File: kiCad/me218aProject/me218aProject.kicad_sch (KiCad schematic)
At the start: 22 parts, among them M1 Motor_Servo, M2 Motor_Servo, M3 Motor_Servo, M4 Motor_Servo, SW1 SW-PB, U1 PIC32MX170F256B, U2 74ACT244, U3 LED_Matrix

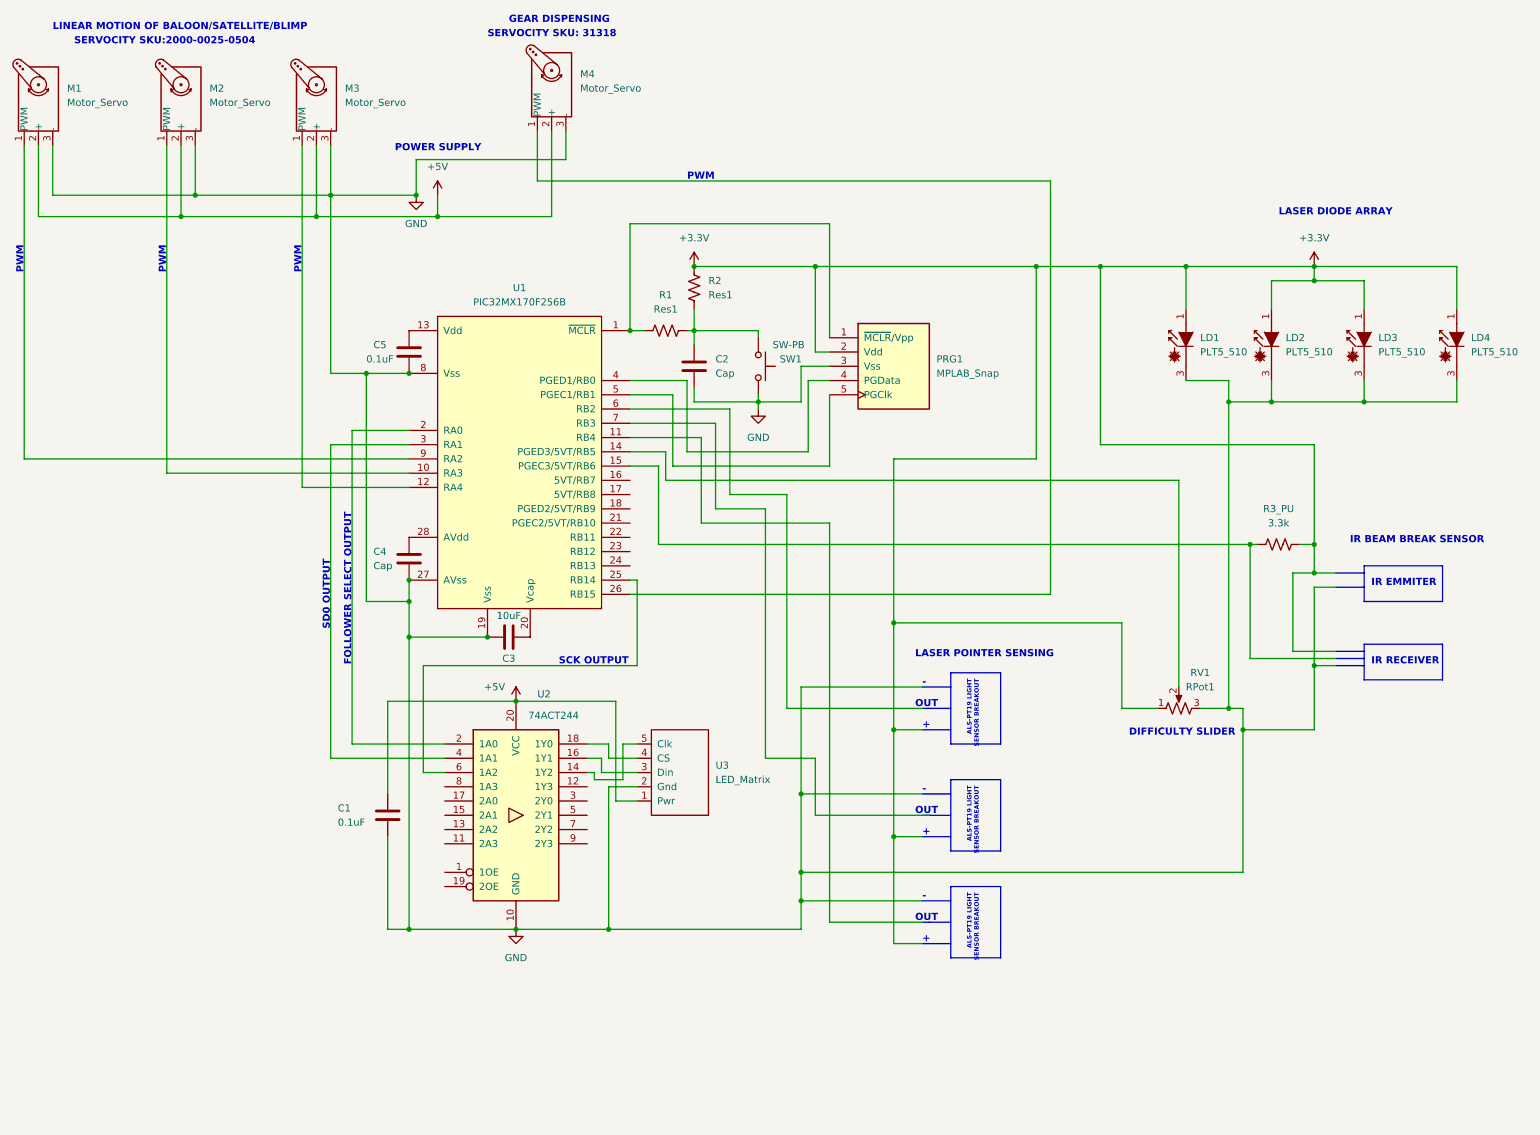
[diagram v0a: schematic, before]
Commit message: Update kiCad based on checkpoint 1 feedback
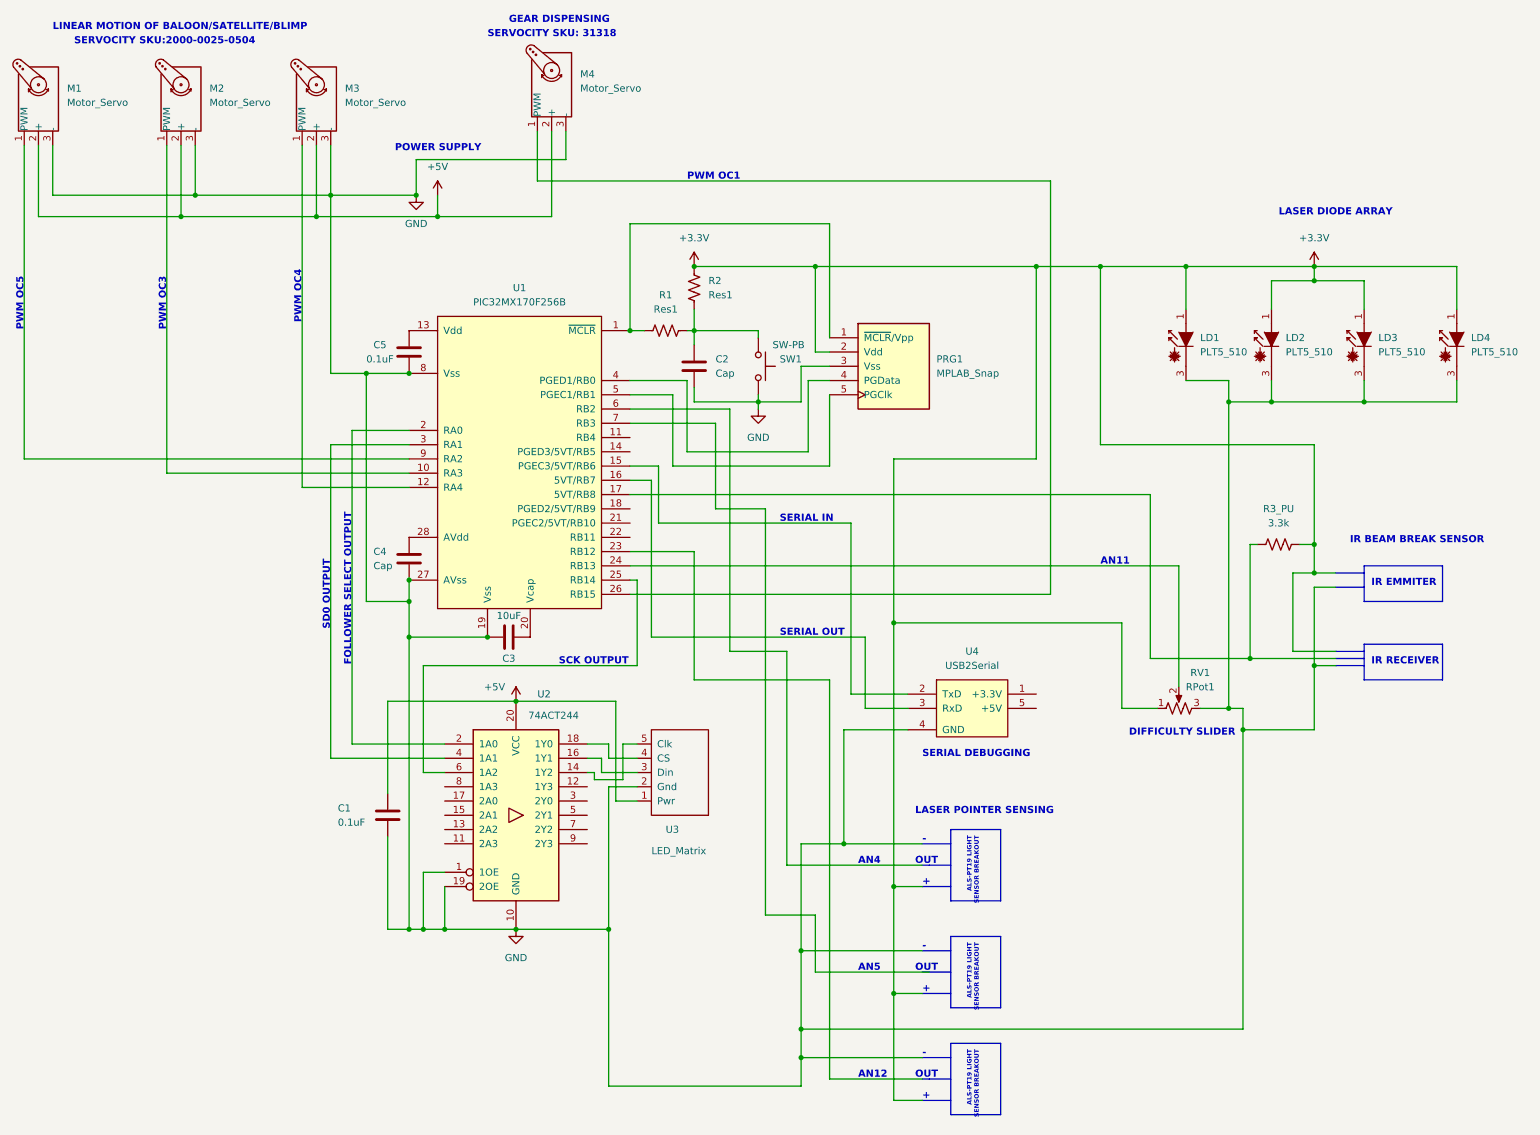
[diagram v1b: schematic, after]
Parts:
- added U4: USB2Serial, symbol ME218_BaseLib:USB2Serial
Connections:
- net GND: now also U2.1 (1OE), U2.19 (2OE), U4.4 (GND)
- net at RV1.2: now also U1.24 (RB13); no longer U1.14 (PGED3/5VT/RB5)
- net at U1.15 (PGEC3/5VT/RB6): now also U4.2 (TxD); no longer R3_PU.1
- net at U1.16 (5VT/RB7): now also U4.3 (RxD)
- net at U1.17 (5VT/RB8): now also R3_PU.1
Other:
- note added: "AN11"
- note added: "AN12"
- note added: "AN4"
- note added: "AN5"
- note added: "PWM OC1"
- note added: "PWM OC3"
- note added: "PWM OC4"
- note added: "PWM OC5"
- note added: "SERIAL DEBUGGING"
- note added: "SERIAL IN"
- note added: "SERIAL OUT"
- note removed: "PWM"
